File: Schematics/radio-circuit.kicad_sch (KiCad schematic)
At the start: 40 parts, among them J1 USB_B_Micro, J2 STDC14, J3 0, U1 USBLC6-2SC6, U2 LD39015M33R, U3 STM32F042C6T6, U4 Si4705-D60-GM, Y1 SG-3030CM

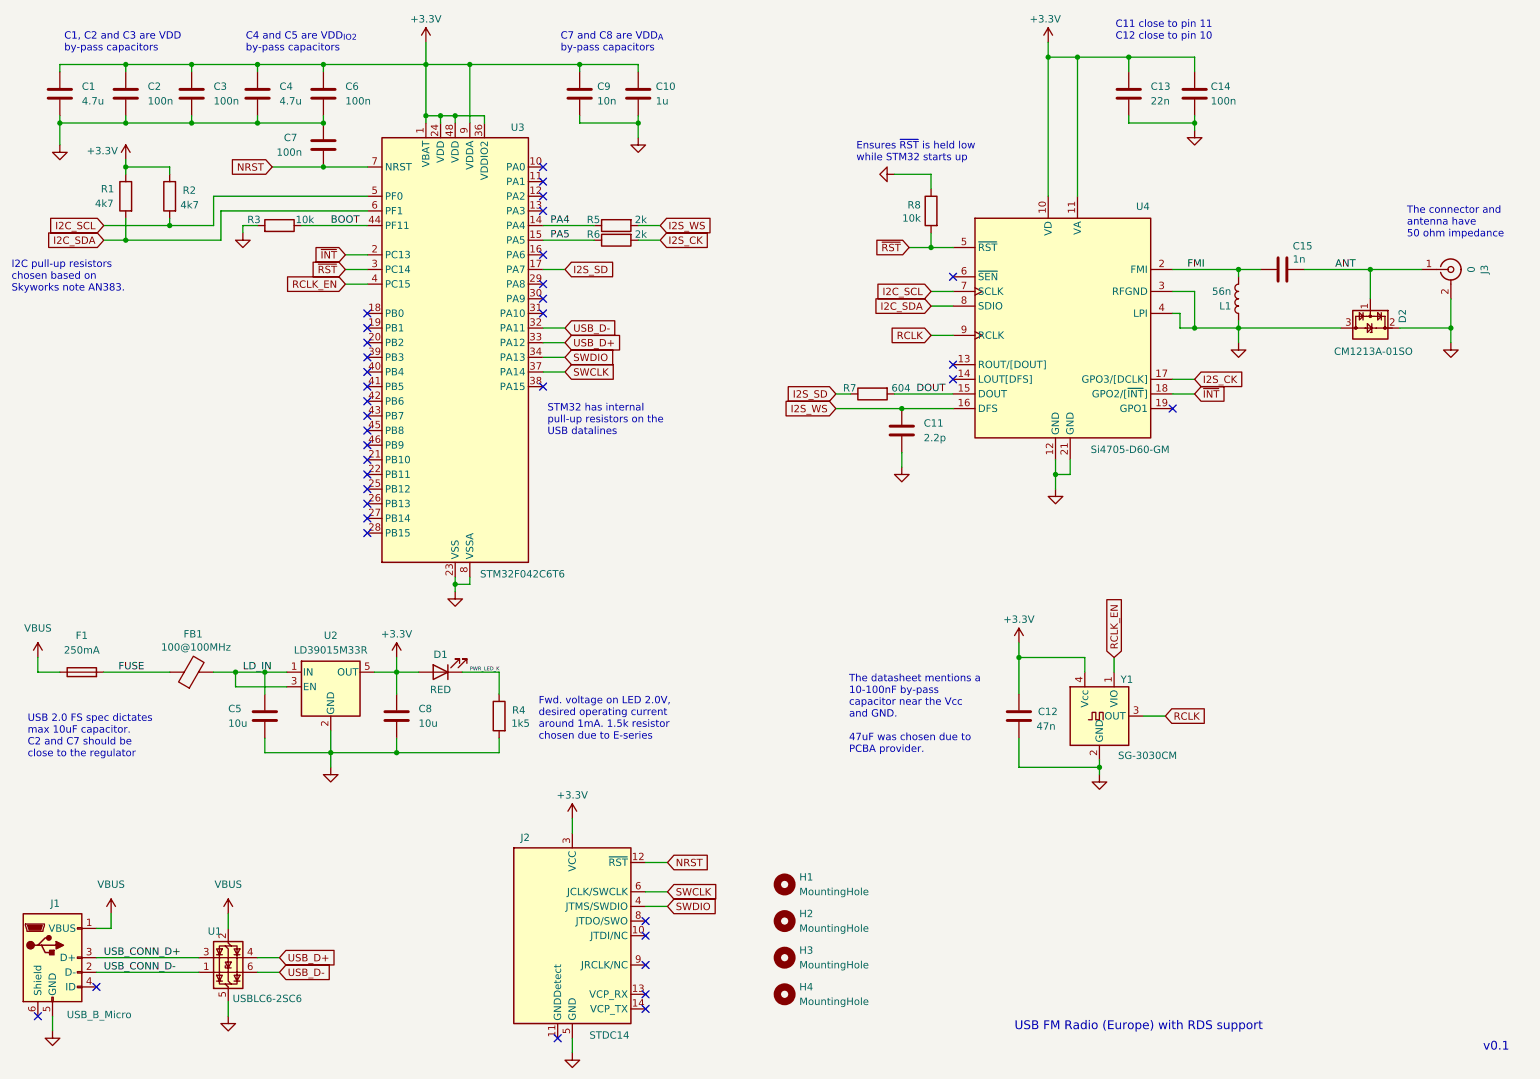
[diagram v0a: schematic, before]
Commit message: Added v0.2 schematic, removed deprecation
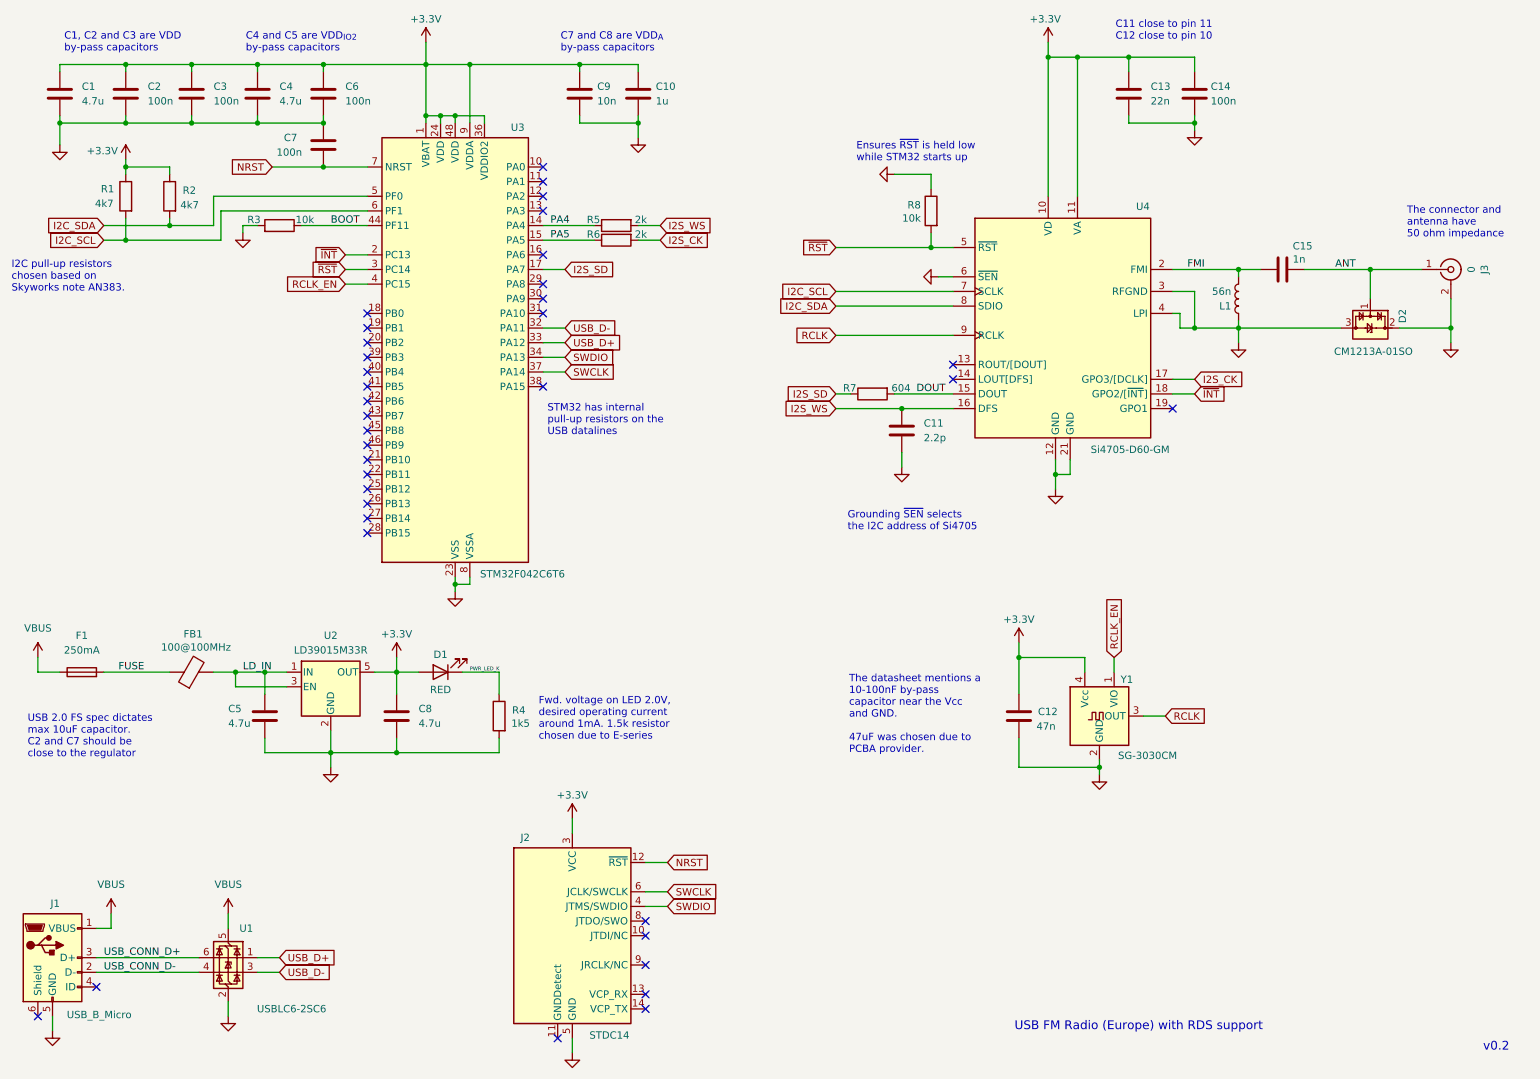
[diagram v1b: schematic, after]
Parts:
- removed H1, H2, H3, H4: MountingHole, MountingHole:MountingHole_3.2mm_M3_ISO7380, symbol Mechanical:MountingHole
- C5, C8: value 10u -> 4.7u; footprint Capacitor_SMD:C_0805_2012Metric -> Capacitor_SMD:C_0603_1608Metric; JLCPCB Part Number C15850 -> C19666
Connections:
- net GND: now also U1.2 (GND), U4.6 (~{SEN}); no longer U1.5 (VBUS)
- net I2C_SCL: now also R1.2, U3.6 (PF1); no longer R2.2, U3.5 (PF0)
- net I2C_SDA: now also R2.2, U3.5 (PF0); no longer R1.2, U3.6 (PF1)
- net USB_CONN_D+: now also U1.6 (I/O1); no longer U1.3 (I/O2)
- net USB_CONN_D-: now also U1.4 (I/O2); no longer U1.1 (I/O1)
- net USB_D+: now also U1.1 (I/O1); no longer U1.4 (I/O2)
- net USB_D-: now also U1.3 (I/O2); no longer U1.6 (I/O1)
- net VBUS: now also U1.5 (VBUS); no longer U1.2 (GND)
- no-connect marks 37 -> 36
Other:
- note added: "Grounding ~{SEN} selects the I2C address of Si4705"
- note added: "v0.2"
- note removed: "v0.1"

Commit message: Added vertical antenna connector library
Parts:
- J3: footprint Connector_Coaxial:SMA_BAT_Wireless_BWSMA-KWE-Z001 -> BWSMA-KE-Z001:SMA_BAT_Wireless_BWSMA-KE-Z001
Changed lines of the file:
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@@
 			)
 		)
-		(property "Footprint" "Connector_Coaxial:SMA_BAT_Wireless_BWSMA-KWE-Z001"
+		(property "Footprint" "BWSMA-KE-Z001:SMA_BAT_Wireless_BWSMA-KE-Z001"
 			(at 262.89 58.42 0)
 			(effects

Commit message: Renamed symbol library
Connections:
- net +3.3V: no longer U4.10 (VD), U4.11 (VA)
- net DOUT: no longer U4.15 (DOUT)
- net FMI: no longer U4.2 (FMI)
- net GND: no longer U4.12 (GND), U4.21 (GND), U4.3 (RFGND), U4.4 (LPI), U4.6 (~{SEN})
- net I2C_SCL: no longer U4.7 (SCLK)
- net I2C_SDA: no longer U4.8 (SDIO)
- net I2S_CK: no longer U4.17 (GPO3/[DCLK])
- net I2S_WS: no longer U4.16 (DFS)
- net RCLK: no longer U4.9 (RCLK)
- net ~{INT}: no longer U4.18 (GPO2/[~{INT}])
- net ~{RST}: no longer U4.5 (~{RST})

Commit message: Renamed footprint library
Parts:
- J3: footprint BWSMA-KE-Z001:SMA_BAT_Wireless_BWSMA-KE-Z001 -> Local:SMA_BAT_Wireless_BWSMA-KE-Z001
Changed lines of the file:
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@@
 			)
 		)
-		(property "Footprint" "BWSMA-KE-Z001:SMA_BAT_Wireless_BWSMA-KE-Z001"
+		(property "Footprint" "Local:SMA_BAT_Wireless_BWSMA-KE-Z001"
 			(at 262.89 58.42 0)
 			(effects

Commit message: Fixed a broken symbol link in the schematic file
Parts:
- U4: symbol Si470x:Si4705-D60-GM -> Local:Si4705-D60-GM
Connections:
- net +3.3V: now also U4.10 (VD), U4.11 (VA)
- net DOUT: now also U4.15 (DOUT)
- net FMI: now also U4.2 (FMI)
- net GND: now also U4.12 (GND), U4.21 (GND), U4.3 (RFGND), U4.4 (LPI), U4.6 (~{SEN})
- net I2C_SCL: now also U4.7 (SCLK)
- net I2C_SDA: now also U4.8 (SDIO)
- net I2S_CK: now also U4.17 (GPO3/[DCLK])
- net I2S_WS: now also U4.16 (DFS)
- net RCLK: now also U4.9 (RCLK)
- net ~{INT}: now also U4.18 (GPO2/[~{INT}])
- net ~{RST}: now also U4.5 (~{RST})
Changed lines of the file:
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@@
 	)
 	(symbol
-		(lib_id "Si470x:Si4705-D60-GM")
+		(lib_id "Local:Si4705-D60-GM")
 		(at 195.58 66.04 0)
 		(unit 1)
